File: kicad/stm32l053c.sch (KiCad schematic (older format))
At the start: 35 parts, among them P1 SWD, P2 PWR, Q1 BC807, SW1 SW_PUSH, SW2 SW_PUSH, SW3 SW_PUSH, U1 STM32L053C8_LQFP48, U2 TLV61225, U3 um66t, Y1 Crystal

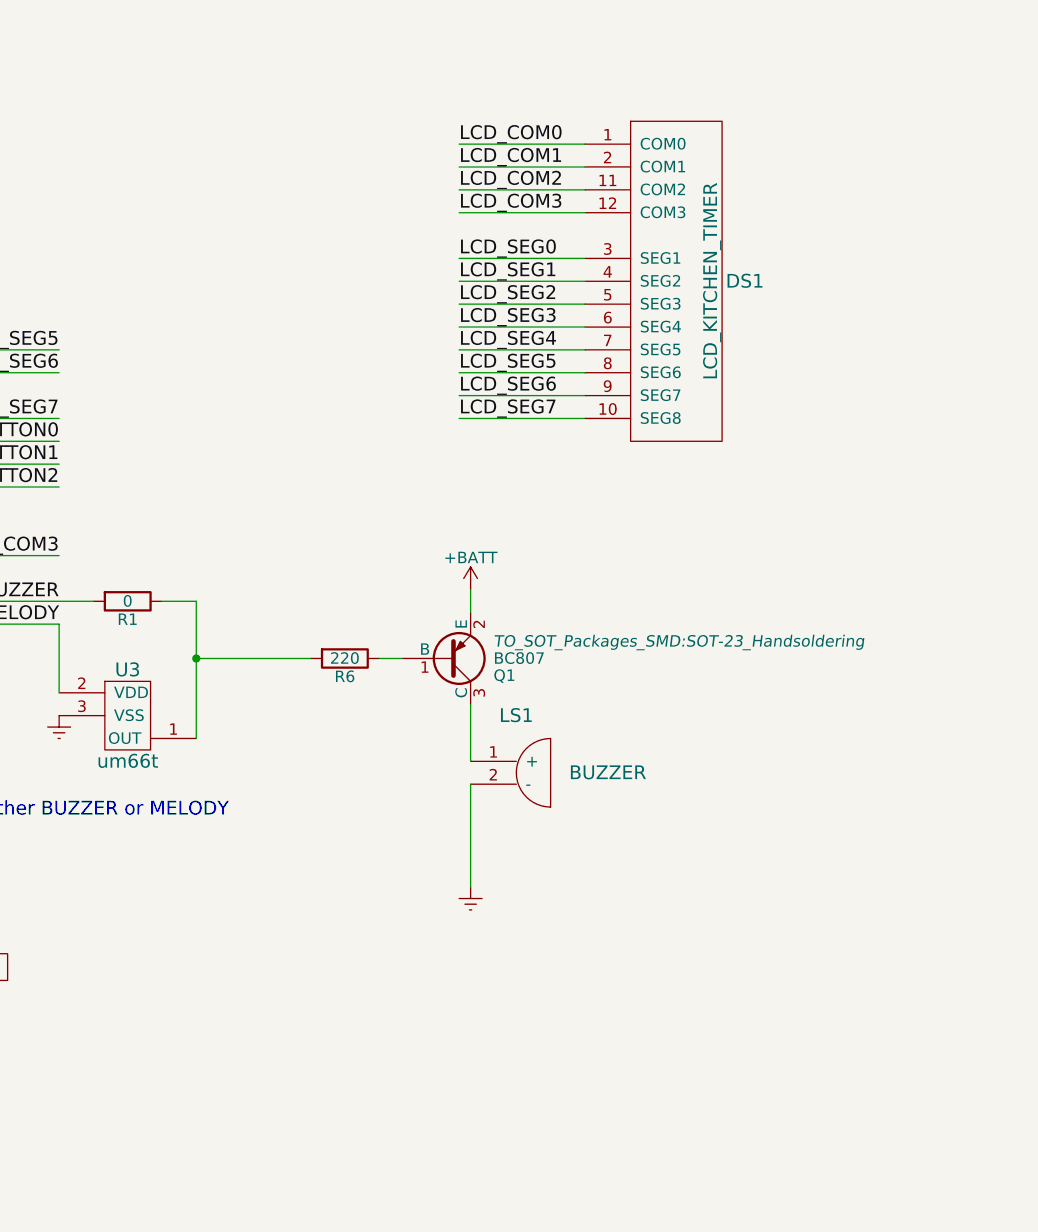
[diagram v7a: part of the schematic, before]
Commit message: The NPN is needed to completely disconnect the buzzer, otherwise it continually uses power
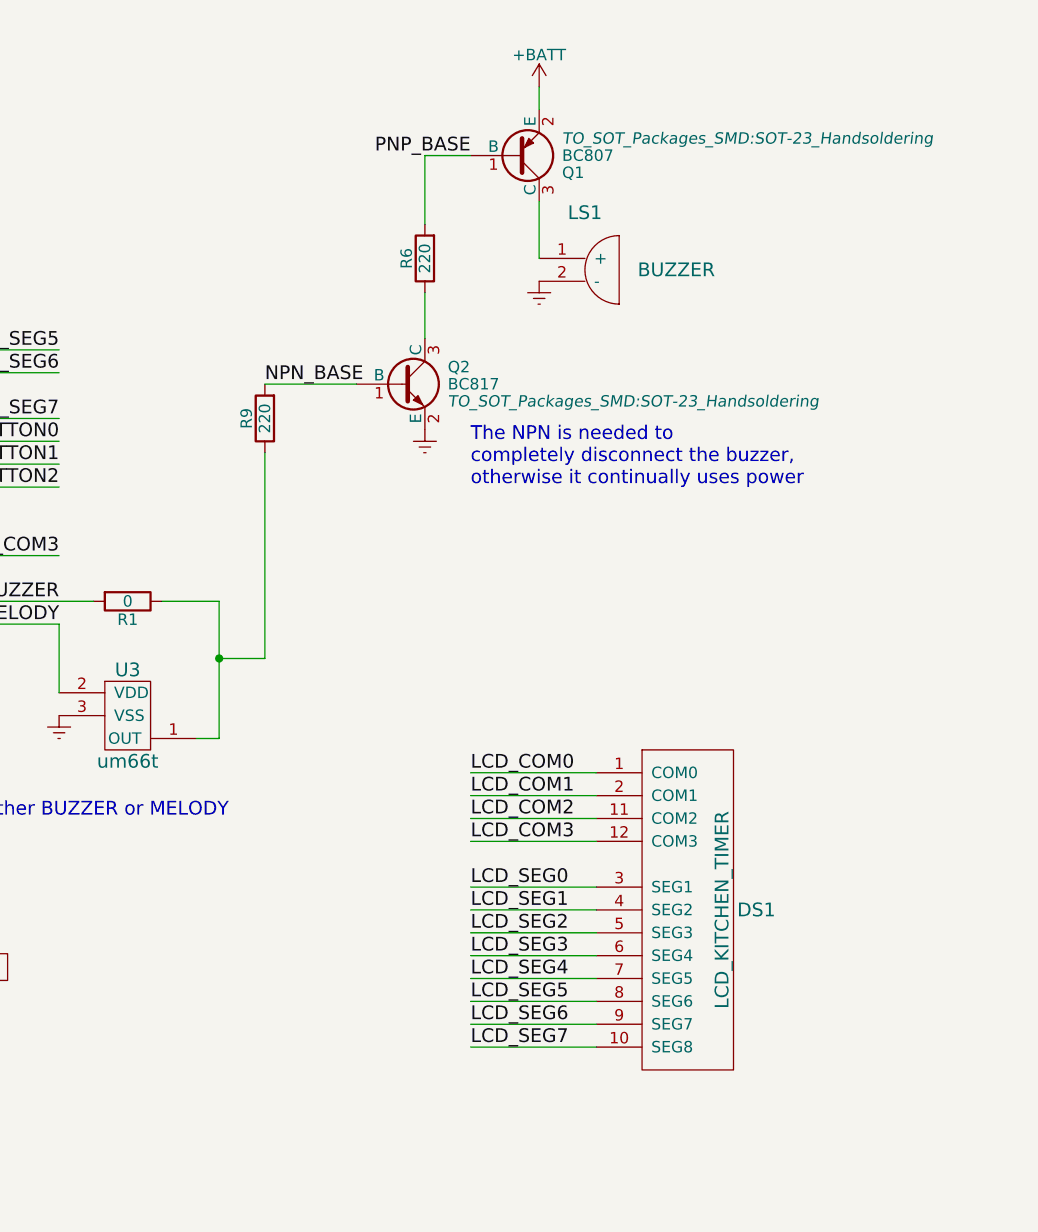
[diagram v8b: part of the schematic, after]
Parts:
- added Q2: BC817, TO_SOT_Packages_SMD:SOT-23_Handsoldering, symbol BC817-40
- added R9: 220, Resistors_SMD:R_0805_HandSoldering, symbol R
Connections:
- net Earth: now also Q2.2 (E)
- net at R6.1: now also Q2.3 (C); no longer Q1.1 (B)
- net at R1.1, U3.1 (OUT): now also R9.1; no longer R6.2
- new net NPN_BASE: Q2.1 (B), R9.2
- new net PNP_BASE: Q1.1 (B), R6.2
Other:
- note added: "The NPN is needed to \ncompletely disconnect the buzzer, \notherwise it continually uses power"
- moved on the sheet: DS1, LS1, Q1, R6
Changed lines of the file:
@@
 OSC32_OUT
 NoConn ~ 4600 4700
-Text Label 8850 1400 0    60   ~ 0
+Text Label 8900 4150 0    60   ~ 0
 LCD_COM0
-Text Label 8850 1500 0    60   ~ 0
+Text Label 8900 4250 0    60   ~ 0
 LCD_COM1
-Text Label 8850 1600 0    60   ~ 0
+Text Label 8900 4350 0    60   ~ 0
 LCD_COM2
-Text Label 8850 1900 0    60   ~ 0
+Text Label 8900 4650 0    60   ~ 0
 LCD_SEG0
-Text Label 8850 2000 0    60   ~ 0
+Text Label 8900 4750 0    60   ~ 0
 LCD_SEG1
-Text Label 8850 2100 0    60   ~ 0
+Text Label 8900 4850 0    60   ~ 0
 LCD_SEG2
-Text Label 8850 2200 0    60   ~ 0
+Text Label 8900 4950 0    60   ~ 0
 LCD_SEG3
-Text Label 8850 2300 0    60   ~ 0
+Text Label 8900 5050 0    60   ~ 0
 LCD_SEG4
-Text Label 8850 2400 0    60   ~ 0
+Text Label 8900 5150 0    60   ~ 0
 LCD_SEG5
-Text Label 8850 2500 0    60   ~ 0
+Text Label 8900 5250 0    60   ~ 0
 LCD_SEG6
-Text Label 8850 2600 0    60   ~ 0
+Text Label 8900 5350 0    60   ~ 0
 LCD_SEG7
-Text Label 8850 1700 0    60   ~ 0
+Text Label 8900 4450 0    60   ~ 0
 LCD_COM3
 $Comp
 L LCD_KITCHEN_TIMER DS1
 U 1 1 584F1C3C
-P 9850 2000
-F 0 "DS1" V 9850 2250 60  0000 C CNN
-F 1 "LCD_KITCHEN_TIMER" H 9850 2100 60  0000 C CNN
-F 2 "theapi:ZEBRA-12" H 9850 2000 60  0001 C CNN
-F 3 "" H 9850 2000 60  0000 C CNN
-	1    9850 2000
+P 9900 4750
+F 0 "DS1" V 9900 5000 60  0000 C CNN
+F 1 "LCD_KITCHEN_TIMER" H 9900 4850 60  0000 C CNN
+F 2 "theapi:ZEBRA-12" H 9900 4750 60  0001 C CNN
+F 3 "" H 9900 4750 60  0000 C CNN
+	1    9900 4750
 	0    1    1    0
 $EndComp
@@
 L BUZZER LS1
 U 1 1 5851ABB3
-P 9100 4150
-F 0 "LS1" H 9100 4400 60  0000 C CNN
-F 1 "BUZZER" H 9500 4150 60  0000 C CNN
-F 2 "Resistors_SMD:R_0805_HandSoldering" H 9250 4400 60  0001 C CNN
-F 3 "" H 9250 4400 60  0001 C CNN
-	1    9100 4150
+P 9400 1950
+F 0 "LS1" H 9400 2200 60  0000 C CNN
+F 1 "BUZZER" H 9800 1950 60  0000 C CNN
+F 2 "Resistors_SMD:R_0805_HandSoldering" H 9550 2200 60  0001 C CNN
+F 3 "" H 9550 2200 60  0001 C CNN
+	1    9400 1950
 	1    0    0    -1
 $EndComp
@@
 L R R6
 U 1 1 5851ADE5
-P 8350 3650
-F 0 "R6" V 8430 3650 50  0000 C CNN
-F 1 "220" V 8350 3650 50  0000 C CNN
-F 2 "Resistors_SMD:R_0805_HandSoldering" V 8280 3650 50  0001 C CNN
-F 3 "" H 8350 3650 50  0000 C CNN
-	1    8350 3650
-	0    1    1    0
+P 8700 1900
+F 0 "R6" V 8780 1900 50  0000 C CNN
+F 1 "220" V 8700 1900 50  0000 C CNN
+F 2 "Resistors_SMD:R_0805_HandSoldering" V 8630 1900 50  0001 C CNN
+F 3 "" H 8700 1900 50  0000 C CNN
+	1    8700 1900
+	-1   0    0    1
 $EndComp
 $Comp
 L Earth #PWR025
 U 1 1 5851B22D
-P 8900 4650
-F 0 "#PWR025" H 8900 4400 50  0001 C CNN
-F 1 "Earth" H 8900 4500 50  0001 C CNN
-F 2 "" H 8900 4650 50  0000 C CNN
-F 3 "" H 8900 4650 50  0000 C CNN
-	1    8900 4650
+P 9200 2000
+F 0 "#PWR025" H 9200 1750 50  0001 C CNN
+F 1 "Earth" H 9200 1850 50  0001 C CNN
+F 2 "" H 9200 2000 50  0000 C CNN
+F 3 "" H 9200 2000 50  0000 C CNN
+	1    9200 2000
 	1    0    0    -1
 $EndComp
@@
 Connection ~ 2700 6550
 Wire Wire Line
-	8850 1400 9400 1400
-Wire Wire Line
-	9400 1500 8850 1500
-Wire Wire Line
-	8850 1600 9400 1600
-Wire Wire Line
-	8850 1700 9400 1700
-Wire Wire Line
-	8850 1900 9400 1900
-Wire Wire Line
-	8850 2000 9400 2000
-Wire Wire Line
-	8850 2100 9400 2100
-Wire Wire Line
-	8850 2200 9400 2200
-Wire Wire Line
-	8850 2300 9400 2300
-Wire Wire Line
-	8850 2400 9400 2400
-Wire Wire Line
-	8850 2500 9400 2500
-Wire Wire Line
-	8850 2600 9400 2600
+	8900 4150 9450 4150
+Wire Wire Line
+	9450 4250 8900 4250
+Wire Wire Line
+	8900 4350 9450 4350
+Wire Wire Line
+	8900 4450 9450 4450
+Wire Wire Line
+	8900 4650 9450 4650
+Wire Wire Line
+	8900 4750 9450 4750
+Wire Wire Line
+	8900 4850 9450 4850
+Wire Wire Line
+	8900 4950 9450 4950
+Wire Wire Line
+	8900 5050 9450 5050
+Wire Wire Line
+	8900 5150 9450 5150
+Wire Wire Line
+	8900 5250 9450 5250
+Wire Wire Line
+	8900 5350 9450 5350
 Wire Wire Line
 	1300 2700 1300 2850
@@
 	2450 2850 3000 2850
 Wire Wire Line
-	8900 4200 8900 4650
-Wire Wire Line
-	8600 3650 8500 3650
-Wire Wire Line
-	7700 3650 8200 3650
+	8700 1450 8900 1450
 Wire Wire Line
 	3400 6550 3700 6550
@@
 	0    1    1    0
 $EndComp
-Wire Wire Line
-	7550 3400 7700 3400
 $Comp
 L D_Schottky D3
@@
 	1    0    0    -1
 $EndComp
-Wire Wire Line
-	7700 3400 7700 4000
-Connection ~ 7700 3650
 Text Notes 6750 4350 0    60   ~ 0
 Either BUZZER or MELODY
 Wire Wire Line
-	8900 3850 8900 4100
+	9200 1650 9200 1900
 $Comp
 L +BATT #PWR029
 U 1 1 586A907B
-P 8900 3350
-F 0 "#PWR029" H 8900 3200 50  0001 C CNN
-F 1 "+BATT" H 8900 3490 50  0000 C CNN
-F 2 "" H 8900 3350 50  0000 C CNN
-F 3 "" H 8900 3350 50  0000 C CNN
-	1    8900 3350
+P 9200 1150
+F 0 "#PWR029" H 9200 1000 50  0001 C CNN
+F 1 "+BATT" H 9200 1290 50  0000 C CNN
+F 2 "" H 9200 1150 50  0000 C CNN
+F 3 "" H 9200 1150 50  0000 C CNN
+	1    9200 1150
 	1    0    0    -1
 $EndComp
@@
 	7100 3500 7100 3800
 Wire Wire Line
-	8900 3450 8900 3350
+	9200 1250 9200 1150
 $Comp
 L R R8
@@
 L BC807-40 Q1
 U 1 1 586C1223
-P 8800 3650
-F 0 "Q1" H 9000 3725 50  0000 L CNN
-F 1 "BC807" H 9000 3650 50  0000 L CNN
-F 2 "TO_SOT_Packages_SMD:SOT-23_Handsoldering" H 9000 3575 50  0000 L CIN
-F 3 "" H 8800 3650 50  0000 L CNN
-	1    8800 3650
+P 9100 1450
+F 0 "Q1" H 9300 1525 50  0000 L CNN
+F 1 "BC807" H 9300 1450 50  0000 L CNN
+F 2 "TO_SOT_Packages_SMD:SOT-23_Handsoldering" H 9300 1375 50  0000 L CIN
+F 3 "" H 9100 1450 50  0000 L CNN
+	1    9100 1450
 	1    0    0    1
 $EndComp
+$Comp
+L BC817-40 Q2
+U 1 1 5875421F
+P 8600 2450
+F 0 "Q2" H 8800 2525 50  0000 L CNN
+F 1 "BC817" H 8800 2450 50  0000 L CNN
+F 2 "TO_SOT_Packages_SMD:SOT-23_Handsoldering" H 8800 2375 50  0000 L CIN
+F 3 "" H 8600 2450 50  0000 L CNN
+	1    8600 2450
+	1    0    0    -1
+$EndComp
+$Comp
+L Earth #PWR030
+U 1 1 5875475A
+P 8700 2650
+F 0 "#PWR030" H 8700 2400 50  0001 C CNN
+F 1 "Earth" H 8700 2500 50  0001 C CNN
+F 2 "" H 8700 2650 50  0000 C CNN
+F 3 "" H 8700 2650 50  0000 C CNN
+	1    8700 2650
+	1    0    0    -1
+$EndComp
+$Comp
+L R R9
+U 1 1 58754819
+P 8000 2600
+F 0 "R9" V 8080 2600 50  0000 C CNN
+F 1 "220" V 8000 2600 50  0000 C CNN
+F 2 "Resistors_SMD:R_0805_HandSoldering" V 7930 2600 50  0001 C CNN
+F 3 "" H 8000 2600 50  0000 C CNN
+	1    8000 2600
+	-1   0    0    1
+$EndComp
+Wire Wire Line
+	8000 2450 8400 2450
+Text Label 8000 2450 0    60   ~ 0
+NPN_BASE
+Wire Wire Line
+	8700 1450 8700 1750
+Wire Wire Line
+	8700 2050 8700 2250
+Text Label 8900 1450 2    60   ~ 0
+PNP_BASE
+Wire Wire Line
+	7550 3400 7800 3400
+Wire Wire Line
+	7800 3400 7800 4000
+Wire Wire Line
+	7800 4000 7700 4000
+Connection ~ 7800 3650
+Text Notes 8900 2900 0    60   ~ 0
+The NPN is needed to \ncompletely disconnect the buzzer, \notherwise it continually uses power
+Wire Wire Line
+	7800 3650 8000 3650
+Wire Wire Line
+	8000 3650 8000 2750
 $EndSCHEMATC
